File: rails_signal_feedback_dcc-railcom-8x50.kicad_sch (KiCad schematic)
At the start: 9 parts, among them Q101 S8550, Q102 S8050, Q103 S8050, Q104 S8550

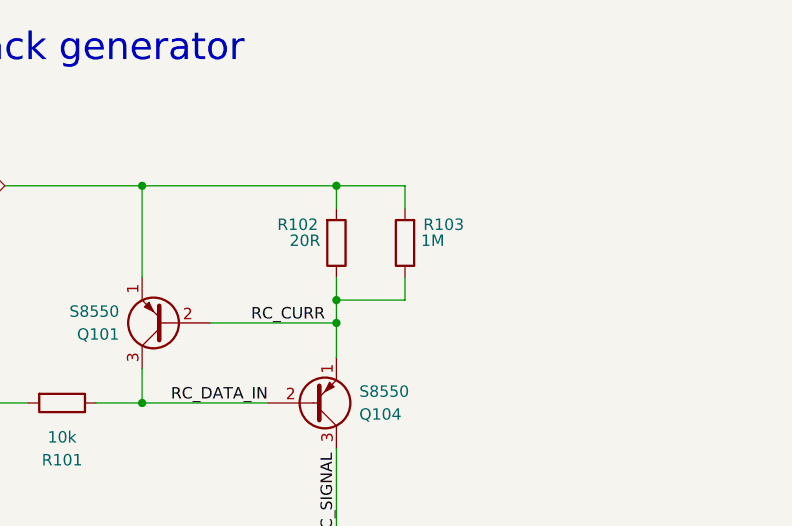
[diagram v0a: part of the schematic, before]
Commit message: Fix - BOM errors
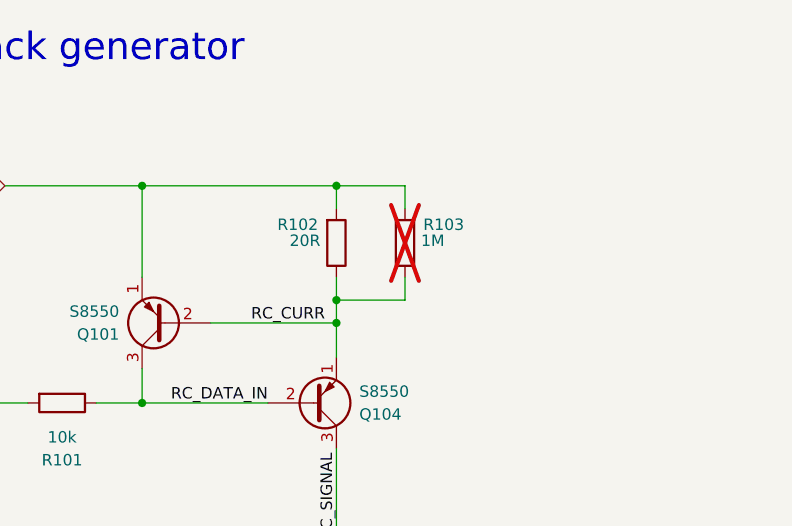
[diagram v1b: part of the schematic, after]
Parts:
- R103: now not fitted
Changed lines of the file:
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@@
 		(in_bom no)
 		(on_board yes)
-		(dnp no)
+		(dnp yes)
 		(property "Reference" "R103"
 			(at 113.792 47.498 0)
